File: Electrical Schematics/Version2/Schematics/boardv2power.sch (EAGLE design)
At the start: 66 parts, among them U1 LM1085_KTT_3, U2 LM1085_KTT_3, U3 LM1084_KTT_3, U4 TPS3514_D_14

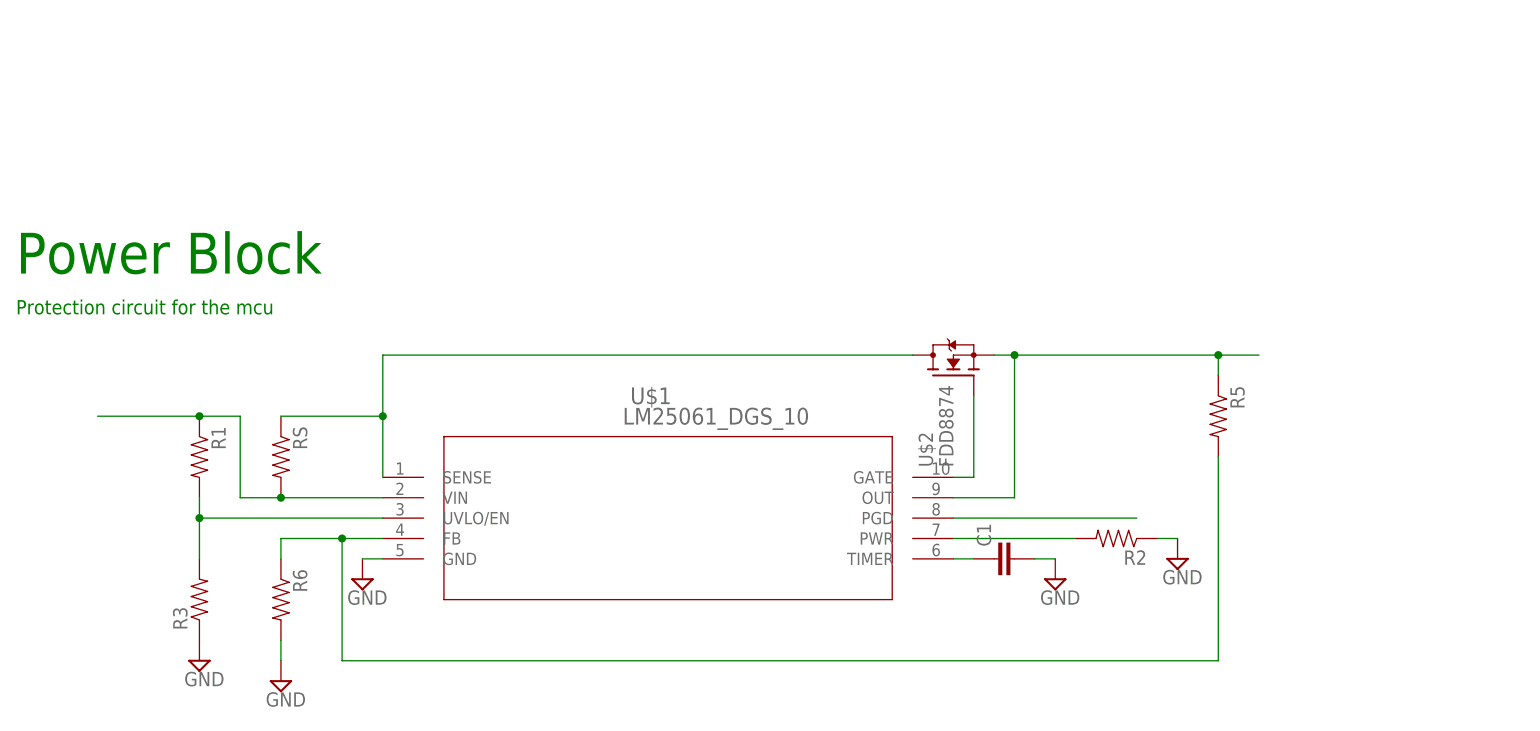
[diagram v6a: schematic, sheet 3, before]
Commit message: cleaned up power
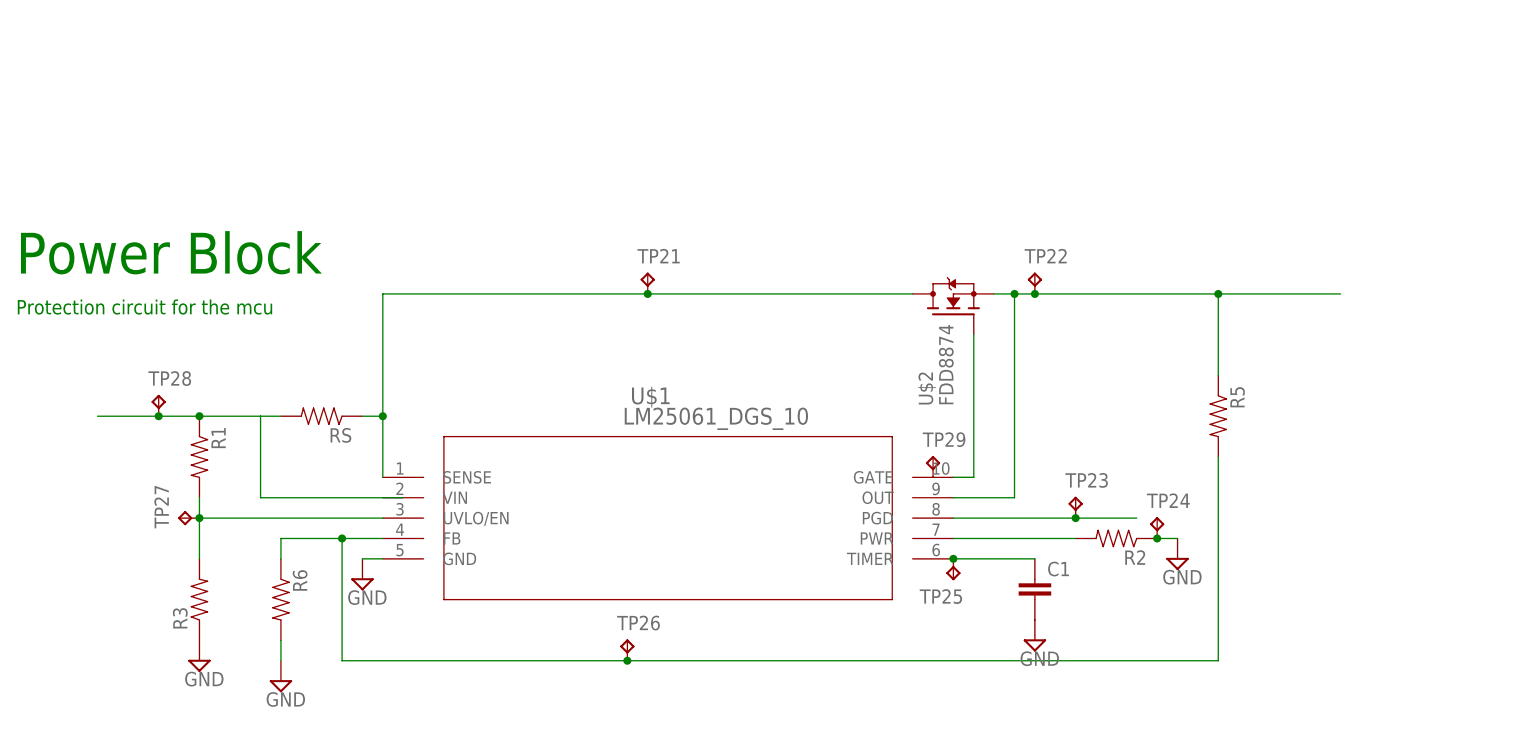
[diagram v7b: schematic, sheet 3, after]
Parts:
- added TP10, TP11, TP12, TP13, TP14, TP15, TP16, TP17, TP18, TP19, TP20, TP21, TP22, TP23, TP24, TP25, TP26, TP27, TP28, TP29, TP9: TPB1,27, testpad:TPB1,27
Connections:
- net N$10 renamed VOLTAGEJMP_+_TO_INPUT_VREG
- net GND: now also TP12.TP, TP24.TP
- net N$1: now also TP25.TP
- net N$17: now also TP11.TP
- net N$19: now also TP9.TP
- net N$20: now also TP16.TP
- net N$21: now also TP10.TP
- net N$22: now also TP13.TP, TP18.TP
- net N$24: now also TP20.TP
- net N$25: now also TP14.TP, TP17.TP
- net N$26: now also TP19.TP
- net N$27: now also TP15.TP
- net N$3: now also TP27.TP
- net N$4: now also TP28.TP; no longer U$1.VIN
- net N$5: now also TP21.TP
- net N$7: now also TP26.TP
- net N$8: now also TP22.TP
- net N$9: now also TP23.TP
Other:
- moved on the sheet: C1, RS, U$2

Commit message: Updated Power
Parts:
- added C11, C12: (no value), eagle-ltspice:CC0603
- added R31, R32, R33: (no value), SparkFun-Passives:RESISTOR0603-RES
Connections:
- new net N$21: C11.1, R19.2, U4.VS5
- new net N$27: R31.2, R32.2, R33.1
- new net N$48: C12.2, R32.1, U4.IS33
- new net N$53: C12.1, R33.2, U4.VS33
- net N$28: now also C11.2
- net N$29: now also R31.1, U4.PGO; no longer R19.2, U4.VS5
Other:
- note added: "3.3V"
- moved on the sheet: C8, R18, R19, R20, TP10, TP12, TP15, TP16, TP19, TP9
